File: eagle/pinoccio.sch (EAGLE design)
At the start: 61 parts, among them IC1 ATMEGA16U2QFN32, J1 AVR_SPI_PRG_6, Q1 16MHz, Q2 32.768k, Q3 16MHz, U1 MCP73831, U2 3.3V, U4 ATMEGA128RFA1, X1 USB-MICROB, Y2 ANTENNA2SMD5

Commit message: more cleanups
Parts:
- C6, C7, C8: value 1uF -> 1.0uF
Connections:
- new net N$25: IC1.PD3(INT3/TXD1), R15.2
- new net N$26: IC1.PD2(INT2/AIN1/RXD1), R8.2
- net RX0: no longer IC1.PD3(INT3/TXD1), R15.2
- net TX0: no longer IC1.PD2(INT2/AIN1/RXD1), R8.2
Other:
- moved on the sheet: D3, R15, R5, R7, R8

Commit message: Updated to v0.7
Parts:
- JP4: device Pinoccio:AVR_SPI_PRG_6PTH -> Pinoccio:AVR_SPI_PRG_6
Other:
- note added: "0.7"
- note removed: "0.6"
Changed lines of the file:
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@@
 <part name="FRAME1" library="Pinoccio" deviceset="FRAME-LETTER" device=""/>
 <part name="C2" library="Pinoccio" deviceset="CAP" device="0402-CAP" value="4.7uF"/>
-<part name="JP4" library="Pinoccio" deviceset="AVR_SPI_PRG_6" device="PTH" value="AVR_SPI"/>
+<part name="JP4" library="Pinoccio" deviceset="AVR_SPI_PRG_6" device="" value="AVR_SPI"/>
 <part name="P+1" library="SparkFun" deviceset="VCC" device=""/>
 <part name="GND1" library="SparkFun" deviceset="GND" device=""/>
@@
 <sheet>
 <plain>
-<text x="238.76" y="1.27" size="2.54" layer="94" font="vector">0.6</text>
+<text x="238.76" y="1.27" size="2.54" layer="94" font="vector">0.7</text>
 <rectangle x1="0.38735" y1="0.29845" x2="0.41275" y2="0.31115" layer="21"/>
 <rectangle x1="0.36195" y1="0.31115" x2="0.45085" y2="0.32385" layer="21"/>

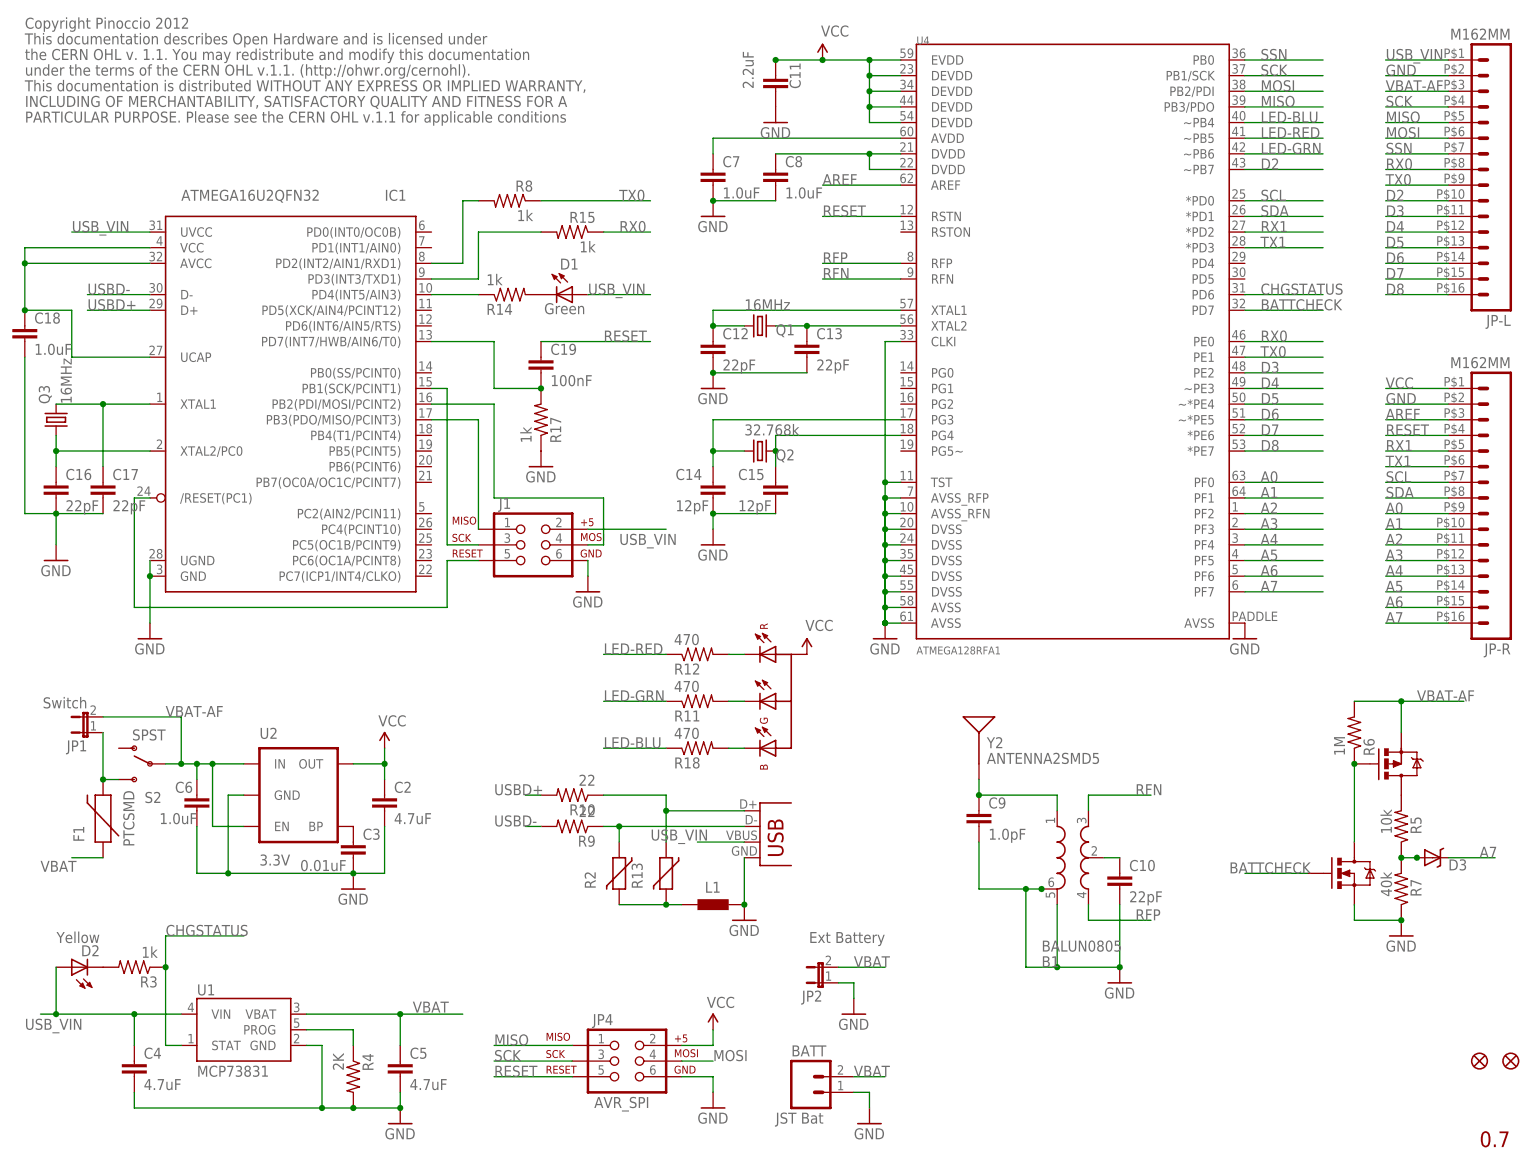
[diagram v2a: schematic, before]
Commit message: Update to v0.9 for lower power regulator, replace MOSFET with dual switch, and other cleanups
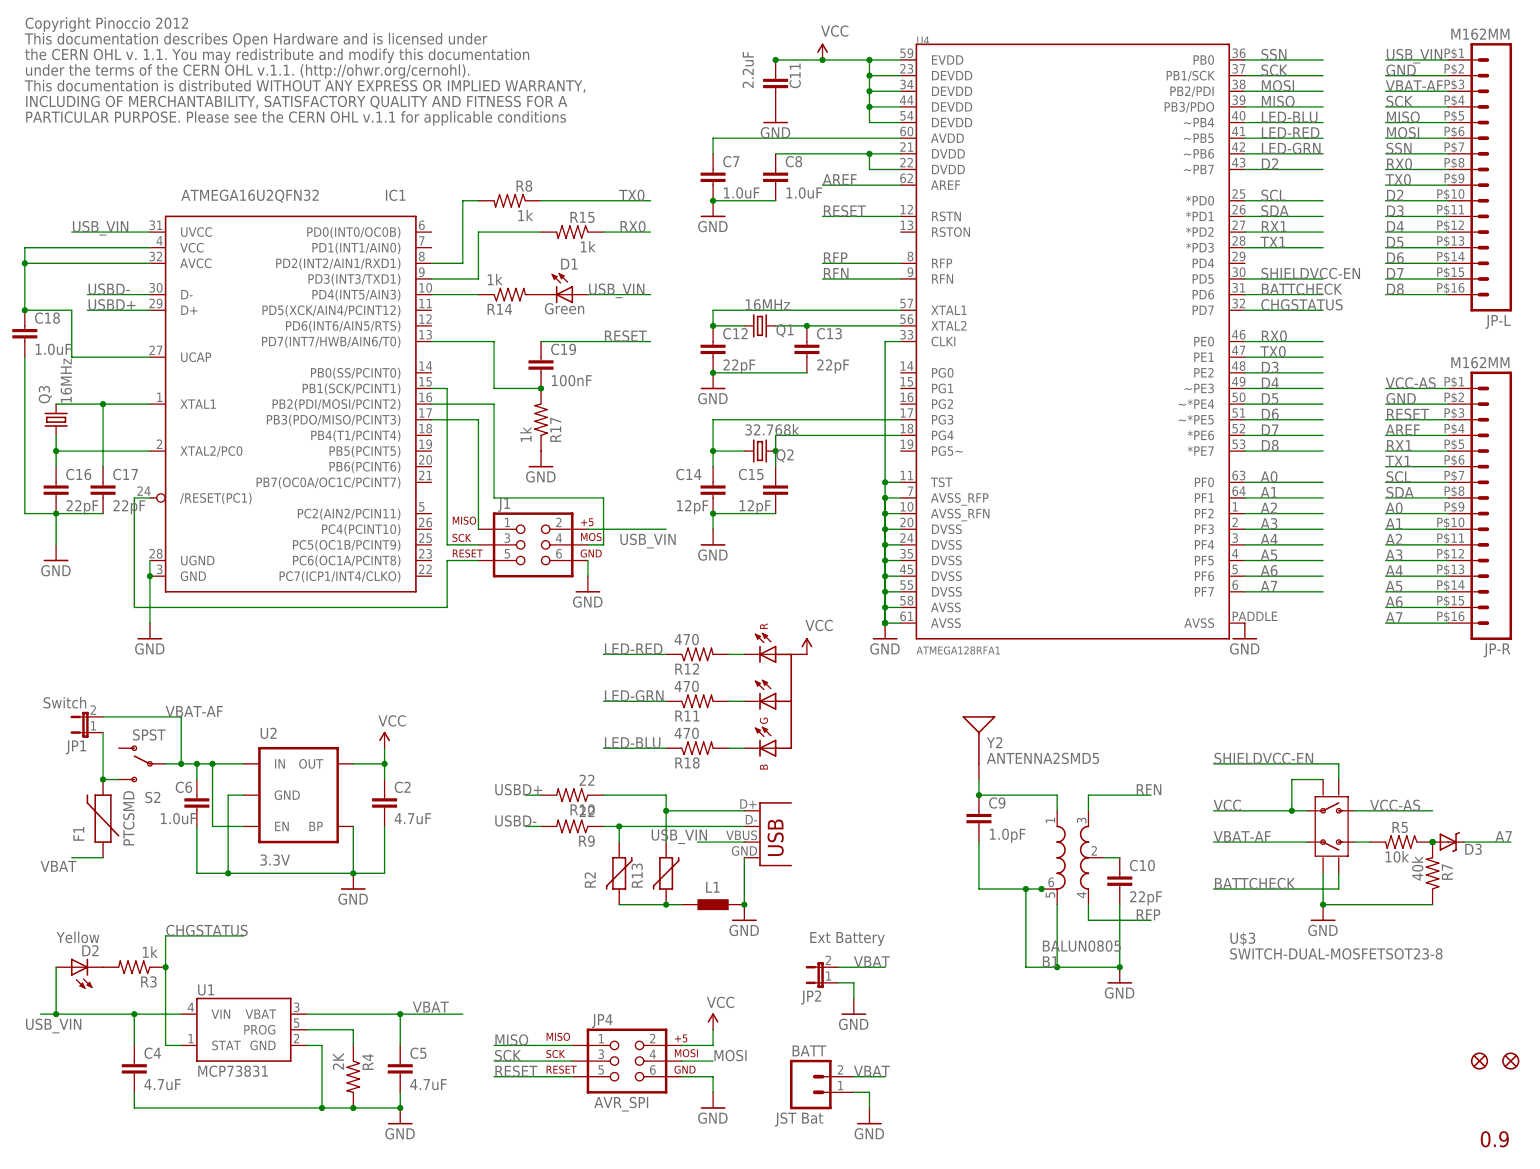
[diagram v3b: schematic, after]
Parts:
- removed C3: 0.01uF, Pinoccio:CAP0402-CAP
- removed R6: 1M, Pinoccio:RESISTOR0402-RES
- removed U$2: MOSFET-DUAL-N-P, Pinoccio:MOSFET-DUAL-N-P
- added U$3: SWITCH-DUAL-MOSFETSOT23-8, Pinoccio:SWITCH-DUAL-MOSFETSOT23-8
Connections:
- removed net N$12: C3.1, U2.BP
- removed net N$7: R6.1, U$2G$N1.D, U$2G$P2.G
- new net SHIELDVCC-EN: U$3.P2-ON1, U4.PD5
- new net VCC-AS: JP-R.1, U$3.P8-VOUT1
- net AREF: now also JP-R.4; no longer JP-R.3
- net BATTCHECK: now also U$3.P3-ON2, U4.PD6; no longer U$2G$N1.G, U4.PD7
- net CHGSTATUS: now also U4.PD7; no longer U4.PD6
- net GND: now also U$3.P6-GND, U2.BP; no longer C3.2, U$2G$N1.S
- net N$3: now also U$3.P5-VOUT2; no longer U$2G$P2.D
- net RESET: now also JP-R.3; no longer JP-R.4
- net VBAT-AF: now also U$3.P4-VIN2; no longer R6.2, U$2G$P2.S
- net VCC: now also U$3.P1-VIN1, U$3.P7-SR; no longer JP-R.1
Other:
- note added: "0.9"
- note removed: "0.7"
- moved on the sheet: D3, R5, R7

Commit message: Update to v0.9
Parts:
- U2: value 3.3V -> TPS78233
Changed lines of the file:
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@@
 <part name="GND1" library="SparkFun" deviceset="GND" device=""/>
 <part name="P+4" library="SparkFun" deviceset="VCC" device=""/>
-<part name="U2" library="SparkFun" deviceset="V_REG_LDO" device="SMD" value="3.3V"/>
+<part name="U2" library="SparkFun" deviceset="V_REG_LDO" device="SMD" value="TPS78233"/>
 <part name="C4" library="Pinoccio" deviceset="CAP" device="0402-CAP" value="4.7uF"/>
 <part name="C5" library="Pinoccio" deviceset="CAP" device="0402-CAP" value="4.7uF"/>

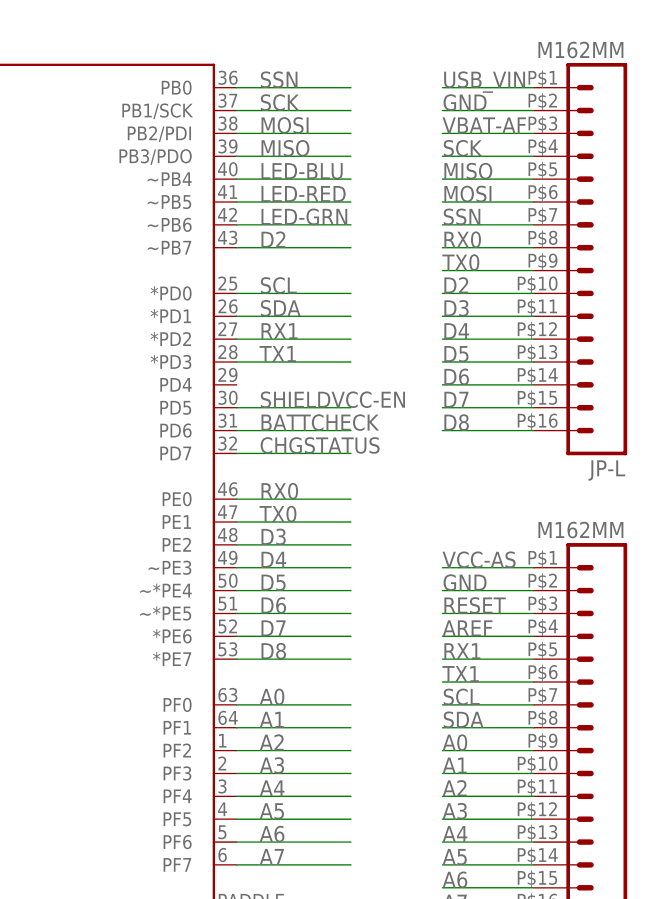
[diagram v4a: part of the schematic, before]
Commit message: Change up header socket pins for better scatter cable adapter support
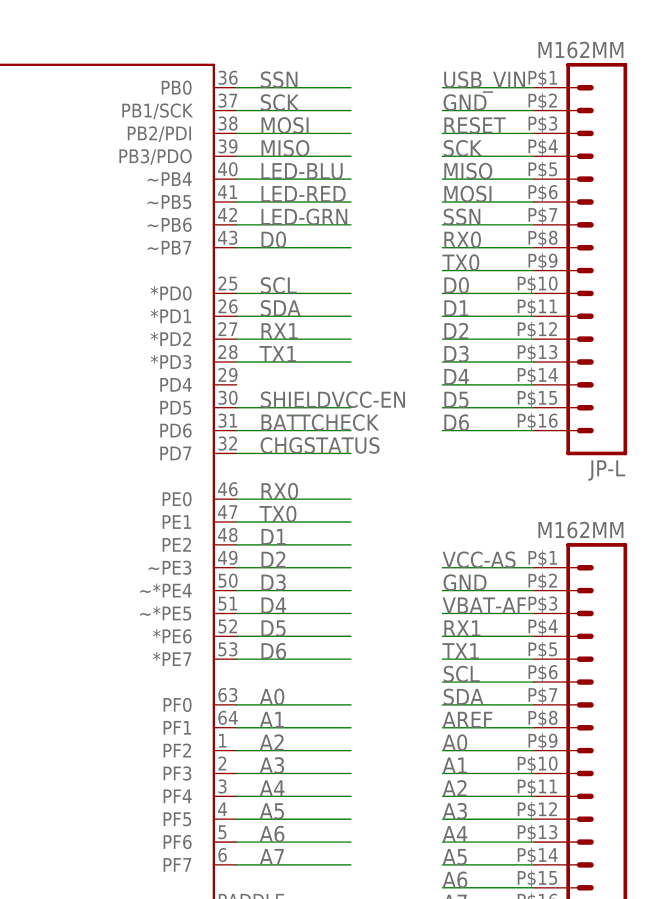
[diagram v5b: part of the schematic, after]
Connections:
- removed net D7: JP-L.15, U4.*PE6
- removed net D8: JP-L.16, U4.*PE7
- new net D0: JP-L.10, U4.~PB7
- new net D1: JP-L.11, U4.PE2
- net AREF: now also JP-R.8; no longer JP-R.4
- net D2: now also JP-L.12, U4.~PE3; no longer JP-L.10, U4.~PB7
- net D3: now also JP-L.13, U4.~*PE4; no longer JP-L.11, U4.PE2
- net D4: now also JP-L.14, U4.~*PE5; no longer JP-L.12, U4.~PE3
- net D5: now also JP-L.15, U4.*PE6; no longer JP-L.13, U4.~*PE4
- net D6: now also JP-L.16, U4.*PE7; no longer JP-L.14, U4.~*PE5
- net RESET: now also JP-L.3; no longer JP-R.3
- net RX1: now also JP-R.4; no longer JP-R.5
- net SCL: now also JP-R.6; no longer JP-R.7
- net SDA: now also JP-R.7; no longer JP-R.8
- net TX1: now also JP-R.5; no longer JP-R.6
- net VBAT-AF: now also JP-R.3; no longer JP-L.3
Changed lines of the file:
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@@
+</segment>
+<segment>
+<pinref part="JP-R" gate="G$1" pin="4"/>
+<wire x1="233.68" y1="116.84" x2="223.52" y2="116.84" width="0.1524" layer="91"/>
+<label x="223.52" y="116.84" size="1.778" layer="95"/>
+</segment>
+</net>
+<net name="TX1" class="0">
+<segment>
+<wire x1="213.36" y1="147.32" x2="200.66" y2="147.32" width="0.1524" layer="91"/>
+<label x="203.2" y="147.32" size="1.778" layer="95"/>
+<pinref part="U4" gate="G$1" pin="*PD3"/>
 </segment>
 <segment>
@@
 </segment>
 </net>
-<net name="TX1" class="0">
-<segment>
-<wire x1="213.36" y1="147.32" x2="200.66" y2="147.32" width="0.1524" layer="91"/>
-<label x="203.2" y="147.32" size="1.778" layer="95"/>
-<pinref part="U4" gate="G$1" pin="*PD3"/>
-</segment>
-<segment>
-<pinref part="JP-R" gate="G$1" pin="6"/>
-<wire x1="233.68" y1="111.76" x2="223.52" y2="111.76" width="0.1524" layer="91"/>
-<label x="223.52" y="111.76" size="1.778" layer="95"/>
-</segment>
-</net>
-<net name="D2" class="0">
+<net name="D0" class="0">
 <segment>
 <pinref part="JP-L" gate="G$1" pin="10"/>
@@
 </segment>
 </net>
-<net name="D3" class="0">
+<net name="D1" class="0">
 <segment>
 <pinref part="JP-L" gate="G$1" pin="11"/>
@@
 </segment>
 </net>
-<net name="D4" class="0">
+<net name="D2" class="0">
 <segment>
 <pinref part="JP-L" gate="G$1" pin="12"/>
@@
 </segment>
 </net>
-<net name="D5" class="0">
+<net name="D3" class="0">
 <segment>
 <pinref part="JP-L" gate="G$1" pin="13"/>
@@
 </segment>
 </net>
-<net name="D6" class="0">
+<net name="D4" class="0">
 <segment>
 <pinref part="JP-L" gate="G$1" pin="14"/>
@@
 </segment>
 </net>
-<net name="D8" class="0">
+<net name="D6" class="0">
 <segment>
 <pinref part="JP-L" gate="G$1" pin="16"/>
@@
 </segment>
 </net>
-<net name="D7" class="0">
+<net name="D5" class="0">
 <segment>
 <pinref part="JP-L" gate="G$1" pin="15"/>
@@
 </segment>
 <segment>
-<pinref part="JP-R" gate="G$1" pin="4"/>
-<wire x1="233.68" y1="116.84" x2="223.52" y2="116.84" width="0.1524" layer="91"/>
-<label x="223.52" y="116.84" size="1.778" layer="95"/>
+<pinref part="JP-R" gate="G$1" pin="8"/>
+<wire x1="233.68" y1="106.68" x2="223.52" y2="106.68" width="0.1524" layer="91"/>
+<label x="223.52" y="106.68" size="1.778" layer="95"/>
 </segment>
 </net>
@@
 </segment>
 <segment>
-<pinref part="JP-L" gate="G$1" pin="3"/>
-<wire x1="233.68" y1="172.72" x2="223.52" y2="172.72" width="0.1524" layer="91"/>
-<label x="223.52" y="172.72" size="1.778" layer="95"/>
-</segment>
-<segment>
 <pinref part="U$3" gate="G$1" pin="P4-VIN2"/>
 <label x="195.58" y="50.8" size="1.778" layer="95"/>
 <wire x1="210.82" y1="50.8" x2="195.58" y2="50.8" width="0.1524" layer="91"/>
+</segment>
+<segment>
+<pinref part="JP-R" gate="G$1" pin="3"/>
+<wire x1="233.68" y1="119.38" x2="223.52" y2="119.38" width="0.1524" layer="91"/>
+<label x="223.52" y="119.38" size="1.778" layer="95"/>
 </segment>
 </net>
@@
 </segment>
 <segment>
+<pinref part="JP-R" gate="G$1" pin="6"/>
+<wire x1="233.68" y1="111.76" x2="223.52" y2="111.76" width="0.1524" layer="91"/>
+<label x="223.52" y="111.76" size="1.778" layer="95"/>
+</segment>
+</net>
+<net name="SDA" class="0">
+<segment>
+<wire x1="213.36" y1="152.4" x2="200.66" y2="152.4" width="0.1524" layer="91"/>
+<pinref part="U4" gate="G$1" pin="*PD1"/>
+<label x="203.2" y="152.4" size="1.778" layer="95"/>
+</segment>
+<segment>
 <pinref part="JP-R" gate="G$1" pin="7"/>
 <wire x1="233.68" y1="109.22" x2="223.52" y2="109.22" width="0.1524" layer="91"/>
@@
 </segment>
 </net>
-<net name="SDA" class="0">
-<segment>
-<wire x1="213.36" y1="152.4" x2="200.66" y2="152.4" width="0.1524" layer="91"/>
-<pinref part="U4" gate="G$1" pin="*PD1"/>
-<label x="203.2" y="152.4" size="1.778" layer="95"/>
-</segment>
-<segment>
-<pinref part="JP-R" gate="G$1" pin="8"/>
-<wire x1="233.68" y1="106.68" x2="223.52" y2="106.68" width="0.1524" layer="91"/>
-<label x="223.52" y="106.68" size="1.778" layer="95"/>
-</segment>
-</net>
 <net name="RX0" class="0">
 <segment>
@@
 </segment>
 <segment>
-<pinref part="JP-R" gate="G$1" pin="3"/>
-<wire x1="233.68" y1="119.38" x2="223.52" y2="119.38" width="0.1524" layer="91"/>
-<label x="223.52" y="119.38" size="1.778" layer="95"/>
-</segment>
-</net>
+<pinref part="JP-L" gate="G$1" pin="3"/>
+<wire x1="233.68" y1="172.72" x2="223.52" y2="172.72" width="0.1524" layer="91"/>
+<label x="223.52" y="172.72" size="1.778" layer="95"/>
+</segment>
+</net>
